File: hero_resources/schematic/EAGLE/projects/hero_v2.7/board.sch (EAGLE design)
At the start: 45 parts

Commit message: Update pcb board version
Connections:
- net GND: no longer MUXP.GND, MUXP.VEE
- net TP_B+: now also TP4056.CE
- net VCC: no longer TP4056.CE

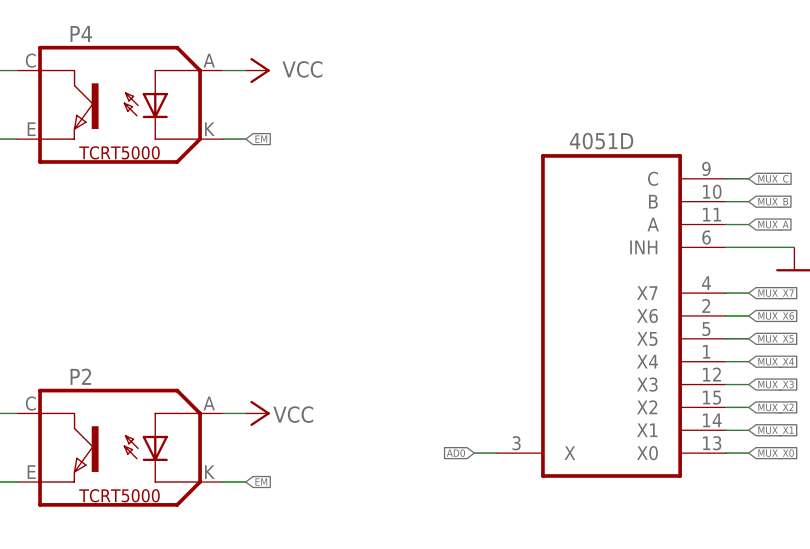
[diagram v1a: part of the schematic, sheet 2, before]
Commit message: Fix unmatching PCB board version 2.7 (issue #22)
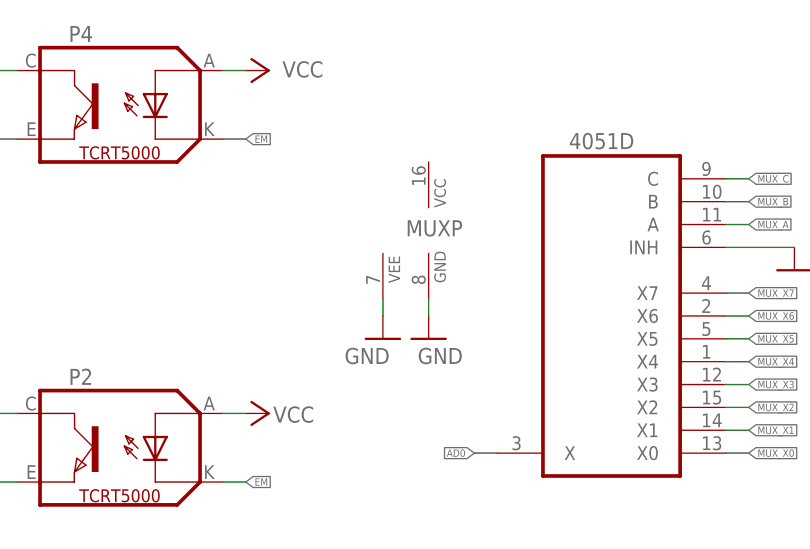
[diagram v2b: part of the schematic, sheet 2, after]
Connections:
- net GND: now also MUXP.GND, MUXP.VEE
- net TP_B+: no longer TP4056.CE
- net VCC: now also TP4056.CE
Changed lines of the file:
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@@
 <part name="R15" library="resistor" library_urn="urn:adsk.eagle:library:348" deviceset="R-EU_" device="R0805" package3d_urn="urn:adsk.eagle:package:23553/2" value="0R"/>
 <part name="BATT1" library="SparkFun-Connectors" library_urn="urn:adsk.eagle:library:513" deviceset="CONN_02" device="JST-PTH-2" package3d_urn="urn:adsk.eagle:package:38053/1"/>
+<part name="GND28" library="supply1" library_urn="urn:adsk.eagle:library:371" deviceset="GND" device=""/>
+<part name="GND29" library="supply1" library_urn="urn:adsk.eagle:library:371" deviceset="GND" device=""/>
+<part name="P+7" library="supply1" library_urn="urn:adsk.eagle:library:371" deviceset="VCC" device=""/>
 </parts>
 <sheets>
@@
 <attribute name="VALUE" x="28.41" y="7.43" size="1.27" layer="96"/>
 </instance>
+<instance part="MUX" gate="P" x="-7.62" y="93.98" smashed="yes">
+<attribute name="NAME" x="-10.16" y="93.345" size="1.778" layer="95"/>
+</instance>
+<instance part="GND28" gate="1" x="-7.62" y="81.95" smashed="yes">
+<attribute name="VALUE" x="-3.81" y="80.934" size="1.778" layer="96" rot="R180"/>
+</instance>
+<instance part="GND29" gate="1" x="-12.7" y="81.95" smashed="yes">
+<attribute name="VALUE" x="-11.938" y="80.934" size="1.778" layer="96" rot="R180"/>
+</instance>
 </instances>
 <busses>
@@
 <pinref part="IRLML2502" gate="G$1" pin="S"/>
 <wire x1="25.89" y1="0.16" x2="25.87" y2="3.62" width="0.1524" layer="91"/>
+</segment>
+<segment>
+<pinref part="GND29" gate="1" pin="GND"/>
+<pinref part="MUX" gate="P" pin="VEE"/>
+<wire x1="-12.7" y1="84.49" x2="-12.7" y2="86.36" width="0.1524" layer="91"/>
+</segment>
+<segment>
+<pinref part="GND28" gate="1" pin="GND"/>
+<pinref part="MUX" gate="P" pin="GND"/>
+<wire x1="-7.62" y1="84.49" x2="-7.62" y2="86.36" width="0.1524" layer="91"/>
 </segment>
 </net>
@@
 <instances>
 <instance part="MT3608" gate="G$1" x="32.2" y="4.3348" smashed="yes"/>
-<instance part="GND13" gate="1" x="24.326" y="2.8108" smashed="yes">
-<attribute name="VALUE" x="24.326" y="0.2708" size="1.778" layer="96" rot="R180"/>
+<instance part="GND13" gate="1" x="23.818" y="2.8108" smashed="yes">
+<attribute name="VALUE" x="26.358" y="2.0488" size="1.778" layer="96" rot="R180"/>
 </instance>
 <instance part="P+5" gate="VCC" x="24.6308" y="17.1872" smashed="yes" rot="R90">
@@
 <attribute name="VALUE" x="107.3286" y="17.6482" size="1.778" layer="96" rot="R180"/>
 </instance>
+<instance part="P+7" gate="VCC" x="-59.7668" y="19.5448" smashed="yes" rot="R270">
+<attribute name="VALUE" x="-59.2588" y="18.0208" size="1.778" layer="96"/>
+</instance>
 </instances>
 <busses>
@@
 <pinref part="MT3608" gate="G$1" pin="GND"/>
 <pinref part="GND13" gate="1" pin="GND"/>
-<wire x1="29.8284" y1="9.5832" x2="24.326" y2="9.4148" width="0.1524" layer="91"/>
-<wire x1="24.326" y1="9.4148" x2="24.326" y2="5.3508" width="0.1524" layer="91"/>
+<wire x1="29.8284" y1="9.5832" x2="23.818" y2="9.4148" width="0.1524" layer="91"/>
+<wire x1="23.818" y1="9.4148" x2="23.818" y2="5.3508" width="0.1524" layer="91"/>
 </segment>
 <segment>
@@
 <junction x="-30.1" y="22.33"/>
 </segment>
+<segment>
+<pinref part="TP4056" gate="G$1" pin="CE"/>
+<pinref part="P+7" gate="VCC" pin="VCC"/>
+<wire x1="-64.1" y1="19.56" x2="-62.3068" y2="19.56" width="0.1524" layer="91"/>
+<wire x1="-62.3068" y1="19.56" x2="-62.3068" y2="19.5448" width="0.1524" layer="91"/>
+</segment>
 </net>
 <net name="STDBY" class="0">
@@
 <net name="TP_B+" class="0">
 <segment>
-<pinref part="TP4056" gate="G$1" pin="CE"/>
-<wire x1="-64.1" y1="19.56" x2="-61.9" y2="19.56" width="0.1524" layer="91"/>
-<label x="-61.85" y="19.55" size="1.778" layer="95" xref="yes"/>
-</segment>
-<segment>
 <pinref part="TP4056" gate="G$1" pin="BAT"/>
